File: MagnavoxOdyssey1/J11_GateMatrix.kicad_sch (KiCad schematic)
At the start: 16 parts

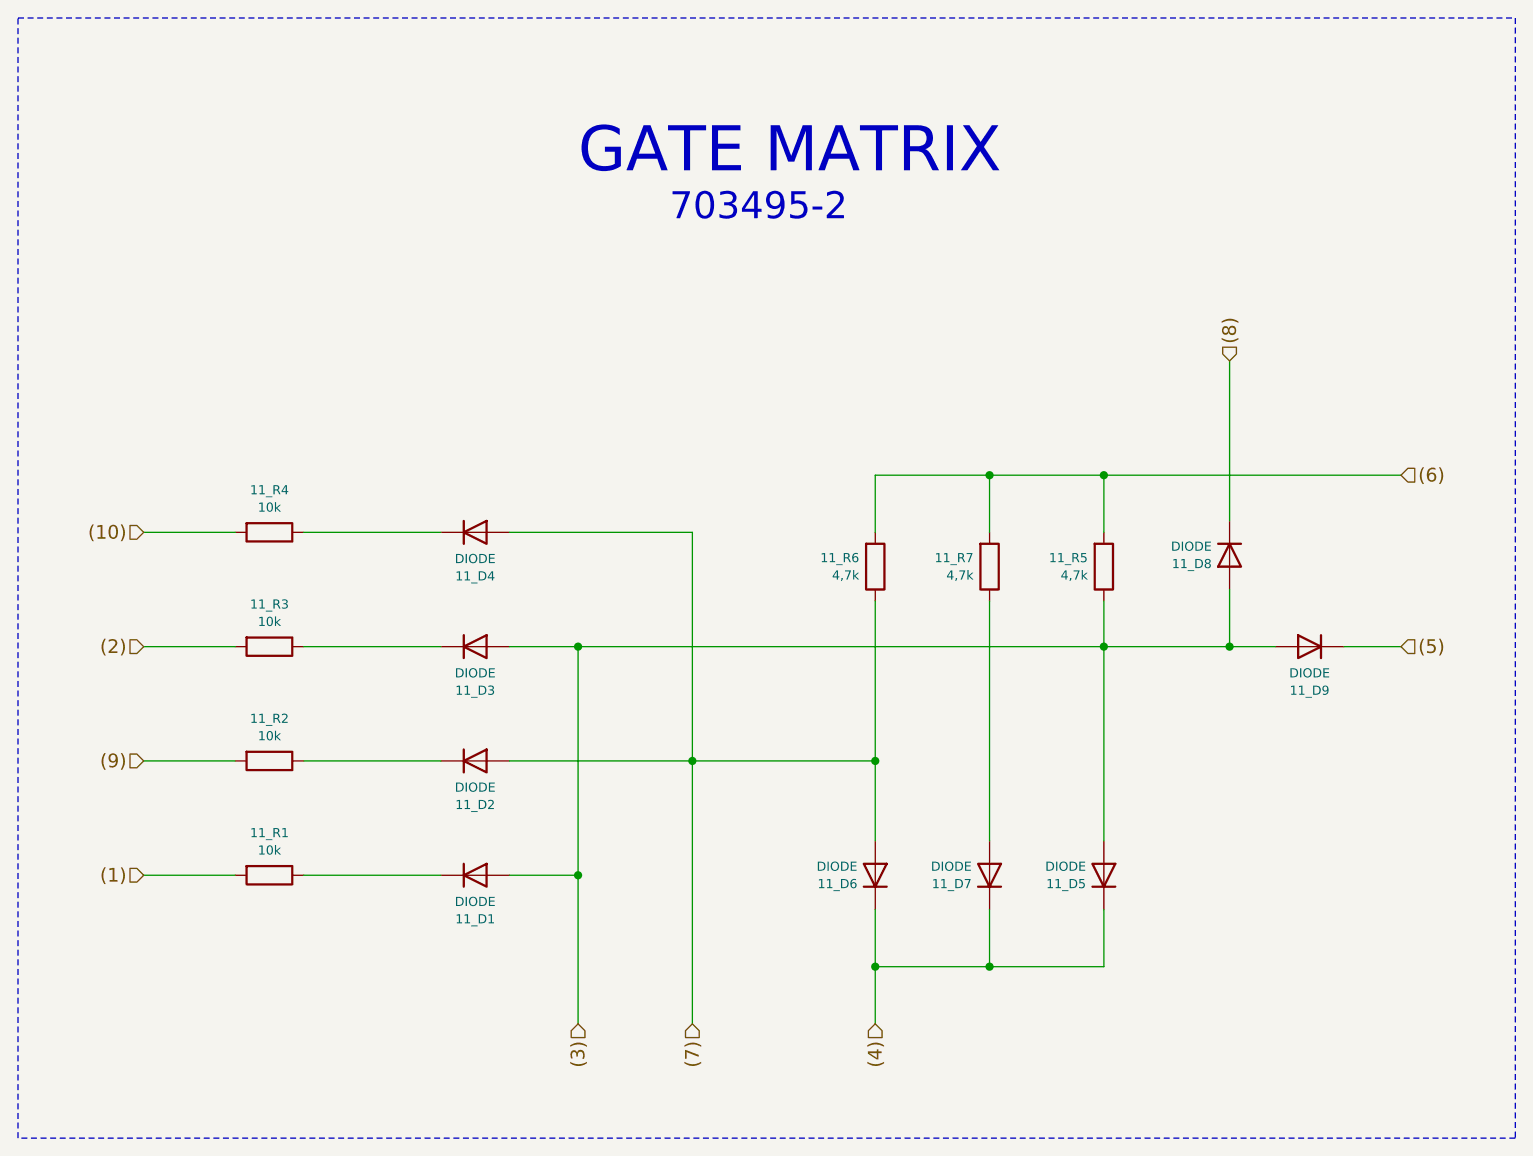
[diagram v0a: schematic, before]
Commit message: update to kicad 9
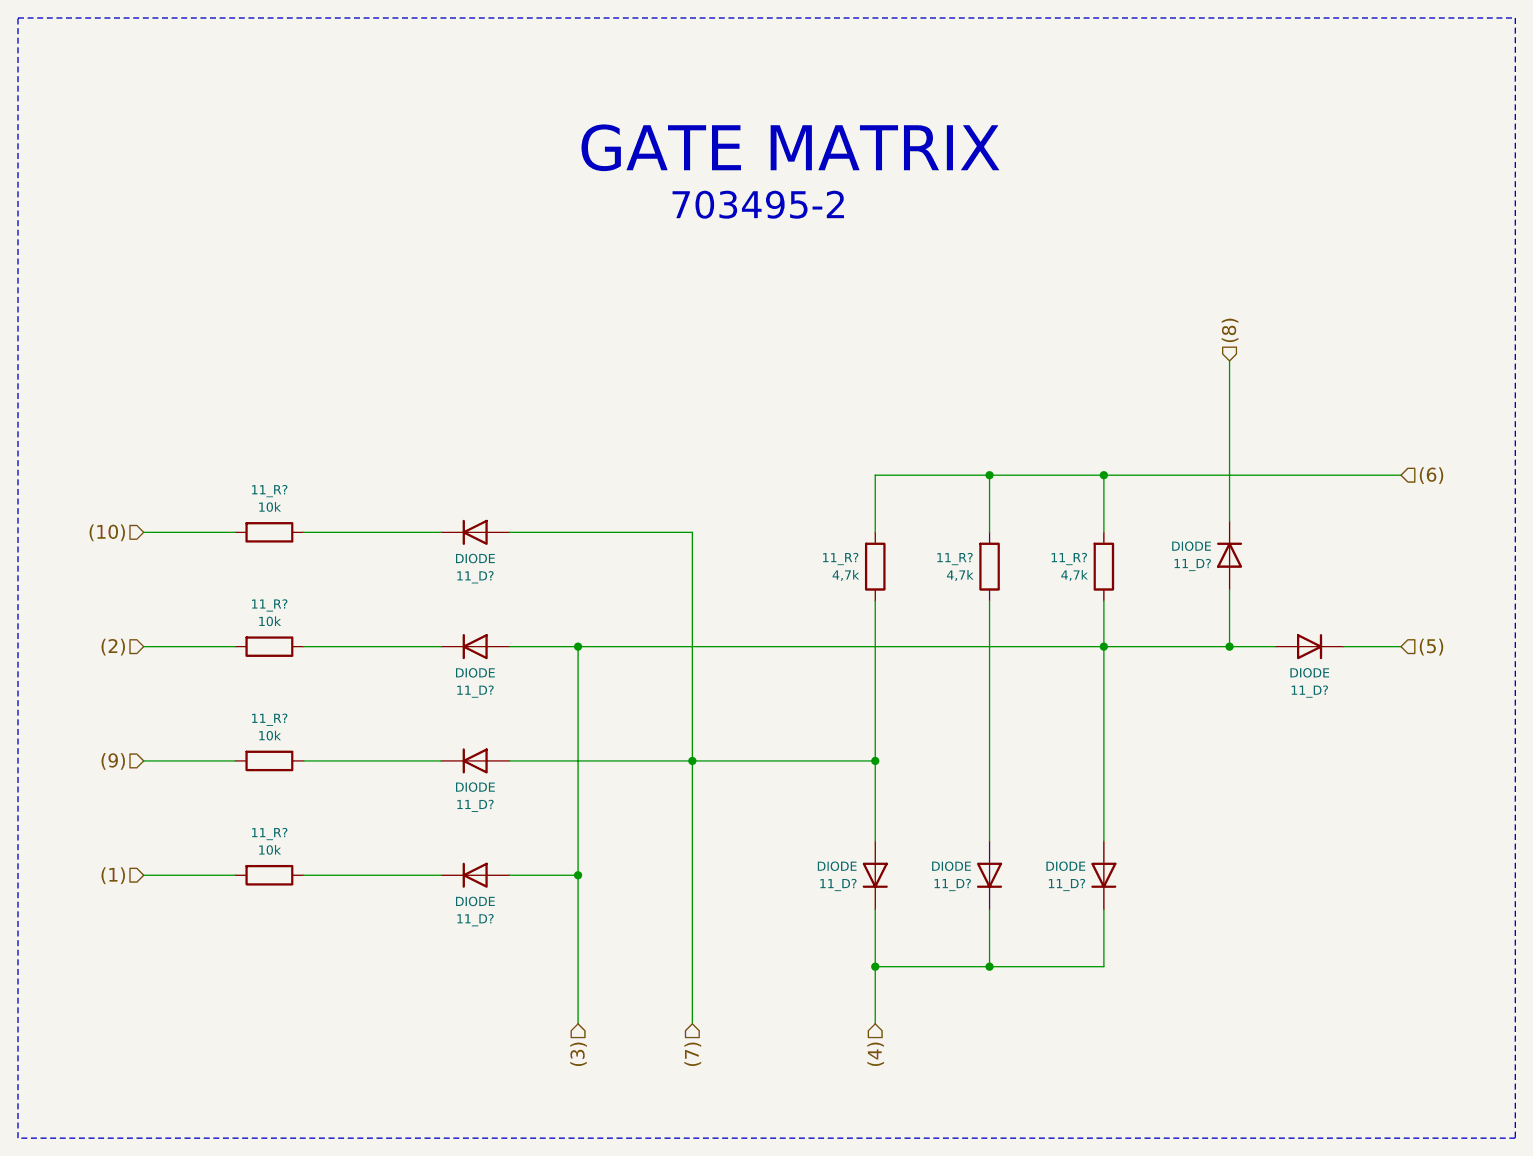
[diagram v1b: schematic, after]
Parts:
- renumbered 11_D4 to 11_D?, 11_D3 to 11_D?, 11_D2 to 11_D?, 11_D1 to 11_D?, 11_D6 to 11_D?, 11_D7 to 11_D?, 11_D5 to 11_D?, 11_D8 to 11_D?, 11_D9 to 11_D?, 11_R4 to 11_R?, 11_R3 to 11_R?, 11_R2 to 11_R?, 11_R1 to 11_R?, 11_R6 to 11_R?, 11_R7 to 11_R?, 11_R5 to 11_R?

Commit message: annotate
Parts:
- gave numbers to parts that had none: 16
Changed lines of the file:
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@@
 		(on_board yes)
 		(dnp no)
-		(property "Reference" "11_R?"
+		(property "Reference" "11_R1"
 			(at 86.36 86.741 90)
 			(effects
@@
 			(project "MagnavoxOdyssey1"
 				(path "/adb6e295-eae5-402e-a614-02a705c3e27c/00000000-0000-0000-0000-0000589216a0"
-					(reference "11_R?")
+					(reference "11_R1")
 					(unit 1)
 				)
@@
 		(on_board yes)
 		(dnp no)
-		(property "Reference" "11_R?"
+		(property "Reference" "11_R5"
 			(at 86.36 99.441 90)
 			(effects
@@
 			(project "MagnavoxOdyssey1"
 				(path "/adb6e295-eae5-402e-a614-02a705c3e27c/00000000-0000-0000-0000-0000589216a0"
-					(reference "11_R?")
+					(reference "11_R5")
 					(unit 1)
 				)
@@
 		(on_board yes)
 		(dnp no)
-		(property "Reference" "11_R?"
+		(property "Reference" "11_R6"
 			(at 86.36 112.141 90)
 			(effects
@@
 			(project "MagnavoxOdyssey1"
 				(path "/adb6e295-eae5-402e-a614-02a705c3e27c/00000000-0000-0000-0000-0000589216a0"
-					(reference "11_R?")
+					(reference "11_R6")
 					(unit 1)
 				)
@@
 		(on_board yes)
 		(dnp no)
-		(property "Reference" "11_R?"
+		(property "Reference" "11_R7"
 			(at 86.36 124.841 90)
 			(effects
@@
 			(project "MagnavoxOdyssey1"
 				(path "/adb6e295-eae5-402e-a614-02a705c3e27c/00000000-0000-0000-0000-0000589216a0"
-					(reference "11_R?")
+					(reference "11_R7")
 					(unit 1)
 				)
@@
 		(on_board yes)
 		(dnp no)
-		(property "Reference" "11_D?"
+		(property "Reference" "11_D1"
 			(at 109.22 96.3168 0)
 			(effects
@@
 			(project "MagnavoxOdyssey1"
 				(path "/adb6e295-eae5-402e-a614-02a705c3e27c/00000000-0000-0000-0000-0000589216a0"
-					(reference "11_D?")
+					(reference "11_D1")
 					(unit 1)
 				)
@@
 		(on_board yes)
 		(dnp no)
-		(property "Reference" "11_D?"
+		(property "Reference" "11_D3"
 			(at 109.22 109.0168 0)
 			(effects
@@
 			(project "MagnavoxOdyssey1"
 				(path "/adb6e295-eae5-402e-a614-02a705c3e27c/00000000-0000-0000-0000-0000589216a0"
-					(reference "11_D?")
+					(reference "11_D3")
 					(unit 1)
 				)
@@
 		(on_board yes)
 		(dnp no)
-		(property "Reference" "11_D?"
+		(property "Reference" "11_D5"
 			(at 109.22 121.7168 0)
 			(effects
@@
 			(project "MagnavoxOdyssey1"
 				(path "/adb6e295-eae5-402e-a614-02a705c3e27c/00000000-0000-0000-0000-0000589216a0"
-					(reference "11_D?")
+					(reference "11_D5")
 					(unit 1)
 				)
@@
 		(on_board yes)
 		(dnp no)
-		(property "Reference" "11_D?"
+		(property "Reference" "11_D6"
 			(at 109.22 134.4168 0)
 			(effects
@@
 			(project "MagnavoxOdyssey1"
 				(path "/adb6e295-eae5-402e-a614-02a705c3e27c/00000000-0000-0000-0000-0000589216a0"
-					(reference "11_D?")
+					(reference "11_D6")
 					(unit 1)
 				)
@@
 		(on_board yes)
 		(dnp no)
-		(property "Reference" "11_R?"
+		(property "Reference" "11_R2"
 			(at 151.892 94.2848 0)
 			(effects
@@
 			(project "MagnavoxOdyssey1"
 				(path "/adb6e295-eae5-402e-a614-02a705c3e27c/00000000-0000-0000-0000-0000589216a0"
-					(reference "11_R?")
+					(reference "11_R2")
 					(unit 1)
 				)
@@
 		(on_board yes)
 		(dnp no)
-		(property "Reference" "11_R?"
+		(property "Reference" "11_R3"
 			(at 164.592 94.2848 0)
 			(effects
@@
 			(project "MagnavoxOdyssey1"
 				(path "/adb6e295-eae5-402e-a614-02a705c3e27c/00000000-0000-0000-0000-0000589216a0"
-					(reference "11_R?")
+					(reference "11_R3")
 					(unit 1)
 				)
@@
 		(on_board yes)
 		(dnp no)
-		(property "Reference" "11_R?"
+		(property "Reference" "11_R4"
 			(at 177.292 94.2848 0)
 			(effects
@@
 			(project "MagnavoxOdyssey1"
 				(path "/adb6e295-eae5-402e-a614-02a705c3e27c/00000000-0000-0000-0000-0000589216a0"
-					(reference "11_R?")
+					(reference "11_R4")
 					(unit 1)
 				)
@@
 		(on_board yes)
 		(dnp no)
-		(property "Reference" "11_D?"
+		(property "Reference" "11_D7"
 			(at 151.6888 130.5052 90)
 			(effects
@@
 			(project "MagnavoxOdyssey1"
 				(path "/adb6e295-eae5-402e-a614-02a705c3e27c/00000000-0000-0000-0000-0000589216a0"
-					(reference "11_D?")
+					(reference "11_D7")
 					(unit 1)
 				)
@@
 		(on_board yes)
 		(dnp no)
-		(property "Reference" "11_D?"
+		(property "Reference" "11_D8"
 			(at 164.3888 130.5052 90)
 			(effects
@@
 			(project "MagnavoxOdyssey1"
 				(path "/adb6e295-eae5-402e-a614-02a705c3e27c/00000000-0000-0000-0000-0000589216a0"
-					(reference "11_D?")
+					(reference "11_D8")
 					(unit 1)
 				)
@@
 		(on_board yes)
 		(dnp no)
-		(property "Reference" "11_D?"
+		(property "Reference" "11_D9"
 			(at 177.0888 130.5052 90)
 			(effects
@@
 			(project "MagnavoxOdyssey1"
 				(path "/adb6e295-eae5-402e-a614-02a705c3e27c/00000000-0000-0000-0000-0000589216a0"
-					(reference "11_D?")
+					(reference "11_D9")
 					(unit 1)
 				)
@@
 		(on_board yes)
 		(dnp no)
-		(property "Reference" "11_D?"
+		(property "Reference" "11_D2"
 			(at 191.0588 94.9452 90)
 			(effects
@@
 			(project "MagnavoxOdyssey1"
 				(path "/adb6e295-eae5-402e-a614-02a705c3e27c/00000000-0000-0000-0000-0000589216a0"
-					(reference "11_D?")
+					(reference "11_D2")
 					(unit 1)
 				)
@@
 		(on_board yes)
 		(dnp no)
-		(property "Reference" "11_D?"
+		(property "Reference" "11_D4"
 			(at 201.93 109.0168 0)
 			(effects
@@
 			(project "MagnavoxOdyssey1"
 				(path "/adb6e295-eae5-402e-a614-02a705c3e27c/00000000-0000-0000-0000-0000589216a0"
-					(reference "11_D?")
-					(unit 1)
-				)
+					(reference "11_D4")
+					(unit 1)
+				)
